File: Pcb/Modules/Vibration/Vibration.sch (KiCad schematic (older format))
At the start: 6 parts, among them J1 JACK_RJ45, P1 C+, P2 C-

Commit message: Update vibration module pcb
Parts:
- removed L1: Ferrite_Bead, Resistors_SMD:R_0805, symbol Ferrite_Bead
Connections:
- wire segments 8 -> 7
- no-connect marks 0 -> 6
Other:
- moved on the sheet: D1, P1, P2, R1
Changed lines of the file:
@@
 LIBS:valves
 LIBS:CA6
+LIBS:Vibration-cache
 EELAYER 25 0
 EELAYER END
@@
 $EndComp
 $Comp
-L GND #PWR1
+L GND #PWR01
 U 1 1 59C40C28
-P 2100 2150
-F 0 "#PWR1" H 2100 1900 50  0001 C CNN
-F 1 "GND" H 2100 2000 50  0000 C CNN
-F 2 "" H 2100 2150 50  0000 C CNN
-F 3 "" H 2100 2150 50  0000 C CNN
-	1    2100 2150
+P 2150 1100
+F 0 "#PWR01" H 2150 850 50  0001 C CNN
+F 1 "GND" H 2150 950 50  0000 C CNN
+F 2 "" H 2150 1100 50  0000 C CNN
+F 3 "" H 2150 1100 50  0000 C CNN
+	1    2150 1100
 	1    0    0    -1
 $EndComp
 $Comp
-L Ferrite_Bead L1
-U 1 1 59C40C66
-P 2100 1900
-F 0 "L1" V 1950 1925 50  0000 C CNN
-F 1 "Ferrite_Bead" V 2250 1900 50  0001 C CNN
-F 2 "Resistors_SMD:R_0805" V 2030 1900 50  0001 C CNN
-F 3 "" H 2100 1900 50  0000 C CNN
-	1    2100 1900
-	1    0    0    -1
-$EndComp
-Wire Wire Line
-	1950 1750 2100 1750
-Wire Wire Line
-	2100 2050 2100 2150
-Wire Wire Line
-	1950 1650 3050 1650
-$Comp
 L R R1
 U 1 1 59C40D7E
-P 2500 1850
-F 0 "R1" V 2580 1850 50  0000 C CNN
-F 1 "1M" V 2500 1850 50  0000 C CNN
-F 2 "Resistors_SMD:R_0603" V 2430 1850 50  0001 C CNN
-F 3 "" H 2500 1850 50  0000 C CNN
-	1    2500 1850
+P 2450 1400
+F 0 "R1" V 2530 1400 50  0000 C CNN
+F 1 "1M" V 2450 1400 50  0000 C CNN
+F 2 "Resistors_SMD:R_0603" V 2380 1400 50  0001 C CNN
+F 3 "" H 2450 1400 50  0000 C CNN
+	1    2450 1400
 	-1   0    0    1
 $EndComp
-Wire Wire Line
-	2100 2100 3050 2100
-Wire Wire Line
-	2500 2100 2500 2000
-Connection ~ 2100 2100
-Wire Wire Line
-	2500 1650 2500 1700
 $Comp
 L D_Schottky D1
 U 1 1 59C40E4B
-P 2800 1850
-F 0 "D1" H 2800 1950 50  0000 C CNN
-F 1 "D_Schottky" H 2800 1750 50  0001 C CNN
-F 2 "Diodes_SMD:D_SOT-23_ANK" H 2800 1850 50  0001 C CNN
-F 3 "" H 2800 1850 50  0000 C CNN
-	1    2800 1850
-	0    1    1    0
+P 2800 1400
+F 0 "D1" H 2800 1500 50  0000 C CNN
+F 1 "D_Schottky" H 2800 1300 50  0001 C CNN
+F 2 "Diodes_SMD:D_SOT-23_ANK" H 2800 1400 50  0001 C CNN
+F 3 "" H 2800 1400 50  0000 C CNN
+	1    2800 1400
+	0    -1   -1   0
 $EndComp
-Wire Wire Line
-	2800 1650 2800 1700
-Connection ~ 2500 1650
-Wire Wire Line
-	2800 2100 2800 2000
-Connection ~ 2500 2100
-Connection ~ 2800 1650
-Connection ~ 2800 2100
 $Comp
 L CONN_01X01 P1
 U 1 1 59C4105F
-P 3250 1650
-F 0 "P1" H 3250 1750 50  0000 C CNN
-F 1 "C+" V 3350 1650 50  0000 C CNN
-F 2 "Wire_Pads:SolderWirePad_single_SMD_5x10mm" H 3250 1650 50  0001 C CNN
-F 3 "" H 3250 1650 50  0000 C CNN
-	1    3250 1650
+P 3200 1650
+F 0 "P1" H 3200 1750 50  0000 C CNN
+F 1 "C+" V 3300 1650 50  0000 C CNN
+F 2 "Wire_Pads:SolderWirePad_single_SMD_5x10mm" H 3200 1650 50  0001 C CNN
+F 3 "" H 3200 1650 50  0000 C CNN
+	1    3200 1650
 	1    0    0    -1
 $EndComp
@@
 L CONN_01X01 P2
 U 1 1 59C410A1
-P 3250 2100
-F 0 "P2" H 3250 2200 50  0000 C CNN
-F 1 "C-" V 3350 2100 50  0000 C CNN
-F 2 "Wire_Pads:SolderWirePad_single_SMD_5x10mm" H 3250 2100 50  0001 C CNN
-F 3 "" H 3250 2100 50  0000 C CNN
-	1    3250 2100
+P 3200 1050
+F 0 "P2" H 3200 1150 50  0000 C CNN
+F 1 "C-" V 3300 1050 50  0000 C CNN
+F 2 "Wire_Pads:SolderWirePad_single_SMD_5x10mm" H 3200 1050 50  0001 C CNN
+F 3 "" H 3200 1050 50  0000 C CNN
+	1    3200 1050
 	1    0    0    -1
 $EndComp
+Wire Wire Line
+	1950 1050 3000 1050
+Wire Wire Line
+	2150 1100 2150 1050
+Connection ~ 2150 1050
+Wire Wire Line
+	2450 1250 2450 1050
+Connection ~ 2450 1050
+Wire Wire Line
+	2800 1250 2800 1050
+Connection ~ 2800 1050
+Wire Wire Line
+	1950 1650 3000 1650
+Wire Wire Line
+	2800 1550 2800 1650
+Connection ~ 2800 1650
+Wire Wire Line
+	2450 1550 2450 1650
+Connection ~ 2450 1650
+NoConn ~ 1950 1150
+NoConn ~ 1950 1250
+NoConn ~ 1950 1350
+NoConn ~ 1950 1450
+NoConn ~ 1950 1550
+NoConn ~ 1950 1750
 $EndSCHEMATC

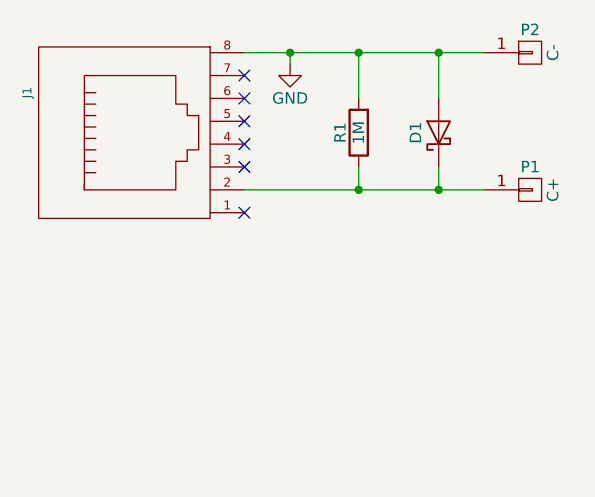
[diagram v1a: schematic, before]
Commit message: Update module pcbs
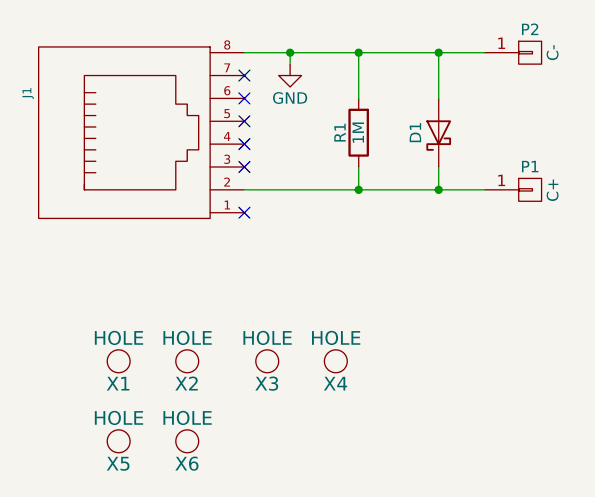
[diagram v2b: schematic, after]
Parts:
- added X1, X2, X5, X6: HOLE, Mounting_Holes:MountingHole_2.5mm_Pad, symbol HOLE
- added X3, X4: HOLE, Mounting_Holes:MountingHole_2.2mm_M2, symbol HOLE
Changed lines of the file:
@@
 NoConn ~ 1950 1550
 NoConn ~ 1950 1750
+$Comp
+L HOLE X1
+U 1 1 5A21F271
+P 1400 2400
+F 0 "X1" H 1400 2300 60  0000 C CNN
+F 1 "HOLE" H 1400 2500 60  0000 C CNN
+F 2 "Mounting_Holes:MountingHole_2.5mm_Pad" H 1400 2400 60  0001 C CNN
+F 3 "" H 1400 2400 60  0000 C CNN
+	1    1400 2400
+	1    0    0    -1
+$EndComp
+$Comp
+L HOLE X2
+U 1 1 5A21F32B
+P 1700 2400
+F 0 "X2" H 1700 2300 60  0000 C CNN
+F 1 "HOLE" H 1700 2500 60  0000 C CNN
+F 2 "Mounting_Holes:MountingHole_2.5mm_Pad" H 1700 2400 60  0001 C CNN
+F 3 "" H 1700 2400 60  0000 C CNN
+	1    1700 2400
+	1    0    0    -1
+$EndComp
+$Comp
+L HOLE X3
+U 1 1 5A21F3A3
+P 2050 2400
+F 0 "X3" H 2050 2300 60  0000 C CNN
+F 1 "HOLE" H 2050 2500 60  0000 C CNN
+F 2 "Mounting_Holes:MountingHole_2.2mm_M2" H 2050 2400 60  0001 C CNN
+F 3 "" H 2050 2400 60  0000 C CNN
+	1    2050 2400
+	1    0    0    -1
+$EndComp
+$Comp
+L HOLE X4
+U 1 1 5A21F3F5
+P 2350 2400
+F 0 "X4" H 2350 2300 60  0000 C CNN
+F 1 "HOLE" H 2350 2500 60  0000 C CNN
+F 2 "Mounting_Holes:MountingHole_2.2mm_M2" H 2350 2400 60  0001 C CNN
+F 3 "" H 2350 2400 60  0000 C CNN
+	1    2350 2400
+	1    0    0    -1
+$EndComp
+$Comp
+L HOLE X5
+U 1 1 5A228D90
+P 1400 2750
+F 0 "X5" H 1400 2650 60  0000 C CNN
+F 1 "HOLE" H 1400 2850 60  0000 C CNN
+F 2 "Mounting_Holes:MountingHole_2.5mm_Pad" H 1400 2750 60  0001 C CNN
+F 3 "" H 1400 2750 60  0000 C CNN
+	1    1400 2750
+	1    0    0    -1
+$EndComp
+$Comp
+L HOLE X6
+U 1 1 5A228DCC
+P 1700 2750
+F 0 "X6" H 1700 2650 60  0000 C CNN
+F 1 "HOLE" H 1700 2850 60  0000 C CNN
+F 2 "Mounting_Holes:MountingHole_2.5mm_Pad" H 1700 2750 60  0001 C CNN
+F 3 "" H 1700 2750 60  0000 C CNN
+	1    1700 2750
+	1    0    0    -1
+$EndComp
 $EndSCHEMATC

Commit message: Update pcb for new switch
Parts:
- D1: symbol D_Schottky -> Device:D_Schottky
- J1: symbol JACK_RJ45 -> CA6:JACK_RJ45
- P1, P2: symbol CONN_01X01 -> Vibration-rescue:CONN_01X01
- R1: symbol R -> Device:R
- X1, X2, X3, X4, X5, X6: symbol HOLE -> CA6:HOLE
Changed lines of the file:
@@
-EESchema Schematic File Version 2
-LIBS:power
-LIBS:device
-LIBS:transistors
-LIBS:conn
-LIBS:linear
-LIBS:regul
-LIBS:74xx
-LIBS:cmos4000
-LIBS:adc-dac
-LIBS:memory
-LIBS:xilinx
-LIBS:microcontrollers
-LIBS:dsp
-LIBS:microchip
-LIBS:analog_switches
-LIBS:motorola
-LIBS:texas
-LIBS:intel
-LIBS:audio
-LIBS:interface
-LIBS:digital-audio
-LIBS:philips
-LIBS:display
-LIBS:cypress
-LIBS:siliconi
-LIBS:opto
-LIBS:atmel
-LIBS:contrib
-LIBS:valves
-LIBS:CA6
+EESchema Schematic File Version 4
 LIBS:Vibration-cache
-EELAYER 25 0
+EELAYER 26 0
 EELAYER END
 $Descr A4 11693 8268
@@
 $EndDescr
 $Comp
-L JACK_RJ45 J1
+L CA6:JACK_RJ45 J1
 U 1 1 59C40B7A
 P 1500 1400
@@
 $EndComp
 $Comp
-L GND #PWR01
+L power:GND #PWR01
 U 1 1 59C40C28
 P 2150 1100
@@
 $EndComp
 $Comp
-L R R1
+L Device:R R1
 U 1 1 59C40D7E
 P 2450 1400
@@
 $EndComp
 $Comp
-L D_Schottky D1
+L Device:D_Schottky D1
 U 1 1 59C40E4B
 P 2800 1400
@@
 $EndComp
 $Comp
-L CONN_01X01 P1
+L Vibration-rescue:CONN_01X01 P1
 U 1 1 59C4105F
 P 3200 1650
@@
 $EndComp
 $Comp
-L CONN_01X01 P2
+L Vibration-rescue:CONN_01X01 P2
 U 1 1 59C410A1
 P 3200 1050
@@
 $EndComp
 Wire Wire Line
-	1950 1050 3000 1050
+	1950 1050 2150 1050
 Wire Wire Line
 	2150 1100 2150 1050
@@
 Connection ~ 2800 1050
 Wire Wire Line
-	1950 1650 3000 1650
+	1950 1650 2450 1650
 Wire Wire Line
 	2800 1550 2800 1650
@@
 NoConn ~ 1950 1750
 $Comp
-L HOLE X1
+L CA6:HOLE X1
 U 1 1 5A21F271
 P 1400 2400
@@
 $EndComp
 $Comp
-L HOLE X2
+L CA6:HOLE X2
 U 1 1 5A21F32B
 P 1700 2400
@@
 $EndComp
 $Comp
-L HOLE X3
+L CA6:HOLE X3
 U 1 1 5A21F3A3
 P 2050 2400
@@
 $EndComp
 $Comp
-L HOLE X4
+L CA6:HOLE X4
 U 1 1 5A21F3F5
 P 2350 2400
@@
 $EndComp
 $Comp
-L HOLE X5
+L CA6:HOLE X5
 U 1 1 5A228D90
 P 1400 2750
@@
 $EndComp
 $Comp
-L HOLE X6
+L CA6:HOLE X6
 U 1 1 5A228DCC
 P 1700 2750
@@
 	1    0    0    -1
 $EndComp
+Wire Wire Line
+	2150 1050 2450 1050
+Wire Wire Line
+	2450 1050 2800 1050
+Wire Wire Line
+	2800 1050 3000 1050
+Wire Wire Line
+	2800 1650 3000 1650
+Wire Wire Line
+	2450 1650 2800 1650
 $EndSCHEMATC
